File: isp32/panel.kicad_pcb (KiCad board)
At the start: 2 copper layers, 73 x 102 mm, 200 parts, among them J1 BAT1, J10 LoRa_ANT, J12 Micro_SD_Card, J2 Switching, J3 USB_C_Receptacle_USB2.0, J4 ESP_JTAG, J5 GPS_ANT, J6 F0, J7 F1, J9 ANT, M1 Motor_Servo, M2 Motor_Servo, M3 Motor_Servo, M4 Motor_Servo, Q1 BSS138, Q2 BSS138, Q3 IRLML6402, Q4 BSS138, Q5 IRLML6402, Q6 S8050, SW1 RST, SW2 IO0, U1 SC189ZSKTRT, U10 BMP280, U11 MPU-9250, U2 USBLC6-2SC6, U3 STM32G030F6, U4 MP1660GTF-Z, U6 24LC32, U7 NEO-XM, U8 ESP32-S3-WROOM-1U, U9 RFM98W-315S2

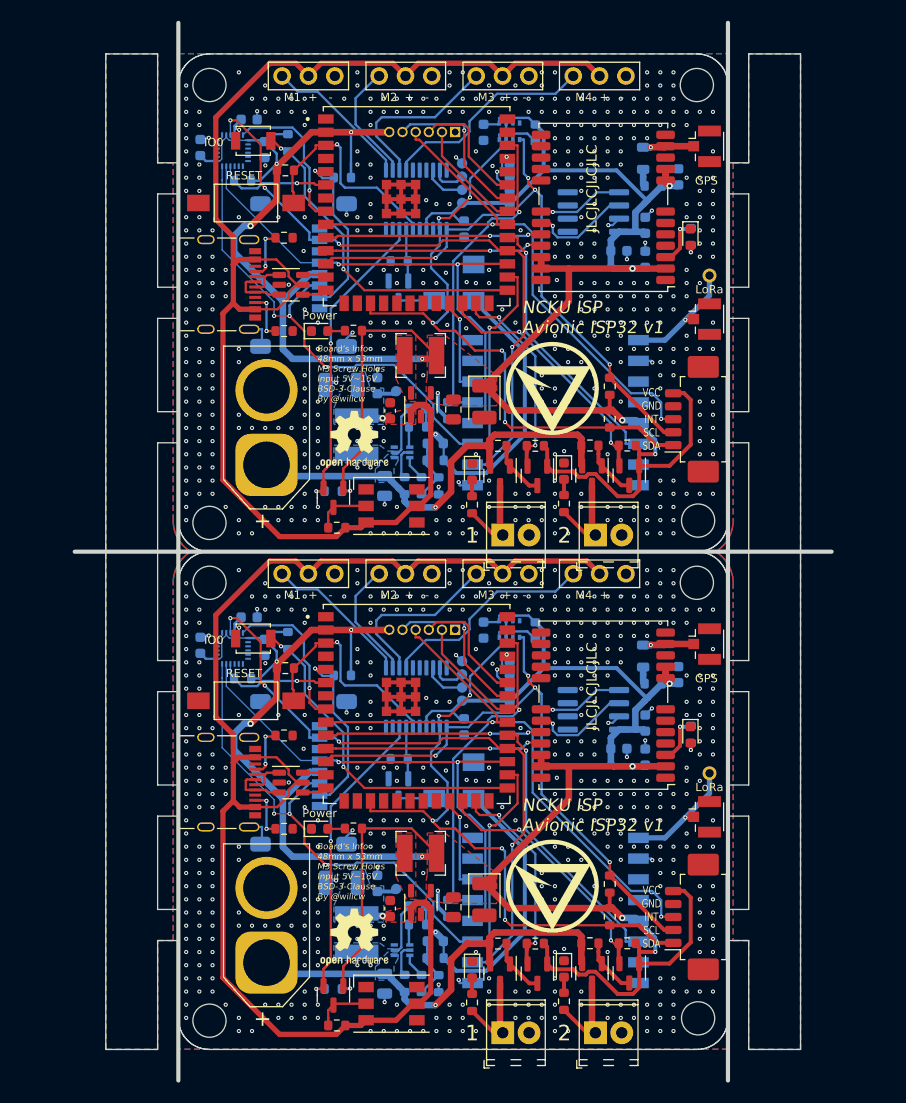
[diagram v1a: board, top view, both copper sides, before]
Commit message: Change label and panel size
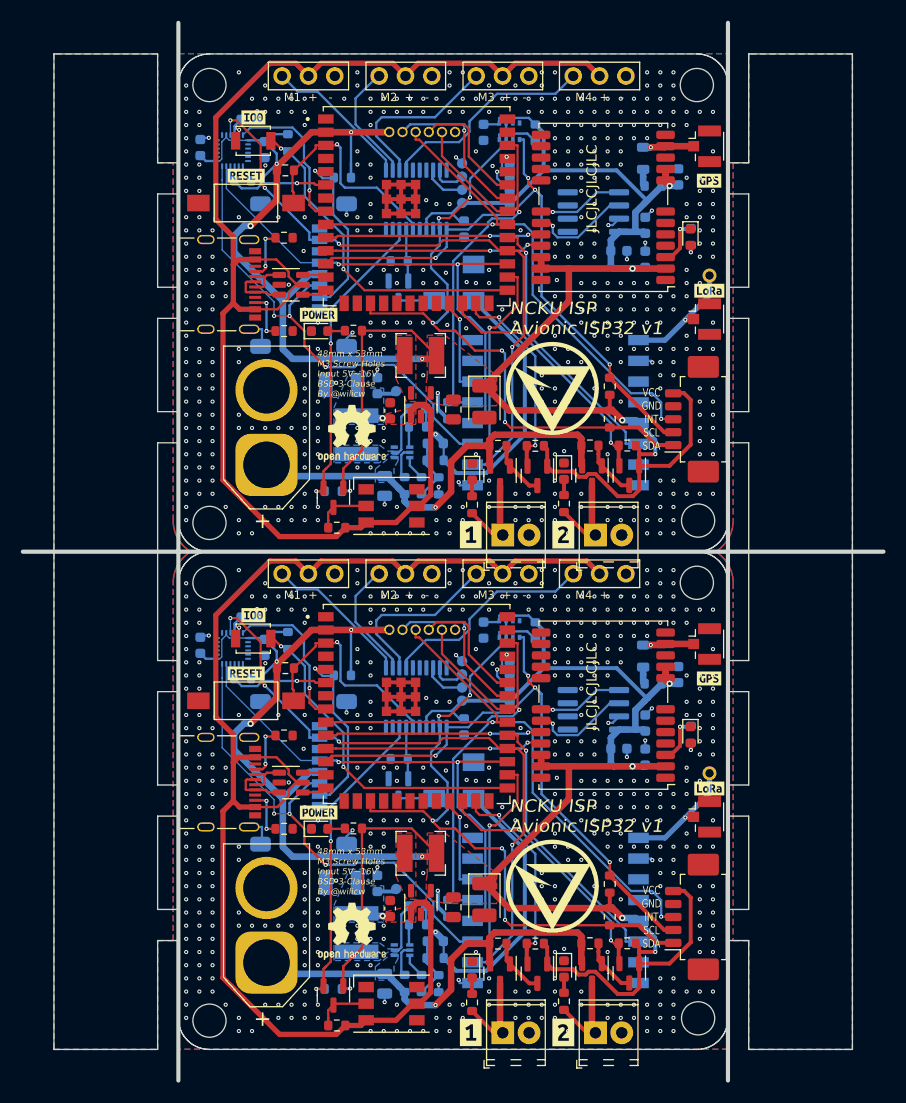
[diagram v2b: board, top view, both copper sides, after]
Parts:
- removed the REF** at (95.5, 57.2)
- removed the REF** at (95.5, 105.2)
- added REF**: OSHW-Logo2_7.3x6mm_SilkScreen, Symbol:OSHW-Logo2_7.3x6mm_SilkScreen, F.Cu at (95.2, 56.6)
- added REF**: OSHW-Logo2_7.3x6mm_SilkScreen, Symbol:OSHW-Logo2_7.3x6mm_SilkScreen, F.Cu at (95.2, 104.6)
- added kibuzzard-63CD04EB: G***, kibuzzard-63CD04EB, F.Cu at (106.7, 114.4)
- added kibuzzard-63CD04EB: G***, kibuzzard-63CD04EB, F.Cu at (106.7, 66.4)
- added kibuzzard-63CD04FB: G***, kibuzzard-63CD04FB, F.Cu at (115.6, 66.4)
- added kibuzzard-63CD04FB: G***, kibuzzard-63CD04FB, F.Cu at (115.6, 114.4)
- added kibuzzard-63CD1CED: G***, kibuzzard-63CD1CED, F.Cu at (85.0, 79.7)
- added kibuzzard-63CD1CED: G***, kibuzzard-63CD1CED, F.Cu at (85.0, 31.7)
- added kibuzzard-63CD1CF7: G***, kibuzzard-63CD1CF7, F.Cu at (85.7, 26.1)
- added kibuzzard-63CD1CF7: G***, kibuzzard-63CD1CF7, F.Cu at (85.7, 74.1)
- added kibuzzard-63CD1D24: G***, kibuzzard-63CD1D24, F.Cu at (92.0, 93.2)
- added kibuzzard-63CD1D24: G***, kibuzzard-63CD1D24, F.Cu at (92.0, 45.2)
- added kibuzzard-63CD1D2E: G***, kibuzzard-63CD1D2E, F.Cu at (129.7, 90.8)
- added kibuzzard-63CD1D2E: G***, kibuzzard-63CD1D2E, F.Cu at (129.7, 42.8)
- added kibuzzard-63CD1D37: G***, kibuzzard-63CD1D37, F.Cu at (129.7, 80.2)
- added kibuzzard-63CD1D37: G***, kibuzzard-63CD1D37, F.Cu at (129.7, 32.2)
- added kibuzzard-63CD1E61: G***, kibuzzard-63CD1E61, B.Cu at (107.8, 82.4)
- added kibuzzard-63CD1E61: G***, kibuzzard-63CD1E61, B.Cu at (112.4, 34.4)
- added kibuzzard-63CD1E61: G***, kibuzzard-63CD1E61, B.Cu at (107.8, 34.4)
- added kibuzzard-63CD1E61: G***, kibuzzard-63CD1E61, B.Cu at (112.4, 82.4)
- added kibuzzard-63CD1E6C: G***, kibuzzard-63CD1E6C, B.Cu at (112.4, 33.1)
- added kibuzzard-63CD1E6C: G***, kibuzzard-63CD1E6C, B.Cu at (112.4, 81.1)
- added kibuzzard-63CD1E76: G***, kibuzzard-63CD1E76, B.Cu at (112.4, 79.9)
- added kibuzzard-63CD1E76: G***, kibuzzard-63CD1E76, B.Cu at (112.4, 31.9)
- added kibuzzard-63CD1E7F: G***, kibuzzard-63CD1E7F, B.Cu at (107.8, 78.5)
- added kibuzzard-63CD1E7F: G***, kibuzzard-63CD1E7F, B.Cu at (107.8, 30.5)
- added kibuzzard-63CD1E7F: G***, kibuzzard-63CD1E7F, B.Cu at (112.4, 30.6)
- added kibuzzard-63CD1E7F: G***, kibuzzard-63CD1E7F, B.Cu at (112.4, 78.6)
- added kibuzzard-63CD1EC0: G***, kibuzzard-63CD1EC0, B.Cu at (107.8, 31.8)
- added kibuzzard-63CD1EC0: G***, kibuzzard-63CD1EC0, B.Cu at (107.8, 79.8)
- added kibuzzard-63CD1EC5: G***, kibuzzard-63CD1EC5, B.Cu at (107.8, 81.1)
- added kibuzzard-63CD1EC5: G***, kibuzzard-63CD1EC5, B.Cu at (107.8, 33.1)
- added kibuzzard-63CD1F56: G***, kibuzzard-63CD1F56, B.Cu at (105.2, 73.6)
- added kibuzzard-63CD1F56: G***, kibuzzard-63CD1F56, B.Cu at (105.2, 25.6)
- added kibuzzard-63CD1F64: G***, kibuzzard-63CD1F64, B.Cu at (103.9, 73.6)
- added kibuzzard-63CD1F64: G***, kibuzzard-63CD1F64, B.Cu at (103.9, 25.6)
- added kibuzzard-63CD1F6A: G***, kibuzzard-63CD1F6A, B.Cu at (102.7, 73.6)
- added kibuzzard-63CD1F6A: G***, kibuzzard-63CD1F6A, B.Cu at (102.7, 25.6)
- added kibuzzard-63CD1F72: G***, kibuzzard-63CD1F72, B.Cu at (101.4, 25.6)
- added kibuzzard-63CD1F72: G***, kibuzzard-63CD1F72, B.Cu at (101.4, 73.6)
- added kibuzzard-63CD1F77: G***, kibuzzard-63CD1F77, B.Cu at (100.1, 25.6)
- added kibuzzard-63CD1F77: G***, kibuzzard-63CD1F77, B.Cu at (100.1, 73.6)
- added kibuzzard-63CD1F7D: G***, kibuzzard-63CD1F7D, B.Cu at (98.8, 25.6)
- added kibuzzard-63CD1F7D: G***, kibuzzard-63CD1F7D, B.Cu at (98.8, 73.6)
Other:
- board size 73 x 102 mm -> 83 x 102 mm
- board text added: "48mm x 53mm M3 Screw Holes Input 5V~16V BSD-3-Clause By @wilicw"
- board text removed: "1"
- board text removed: "2"
- board text removed: "Board's Info 48mm x 53mm M3 Screw Holes Input 5V~16V BSD-3-Clause By @wilicw"
- board text removed: "GND RXD TXD 3V3"
- board text removed: "GND SWCLK SWDIO 3V3"
- board text removed: "GND TDO TMS TCK TDI 3V3"
- board text removed: "GPS"
- board text removed: "IO0"
- board text removed: "LoRa"
- board text removed: "Power"
- board text removed: "RESET"

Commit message: Fix all isp32 issues
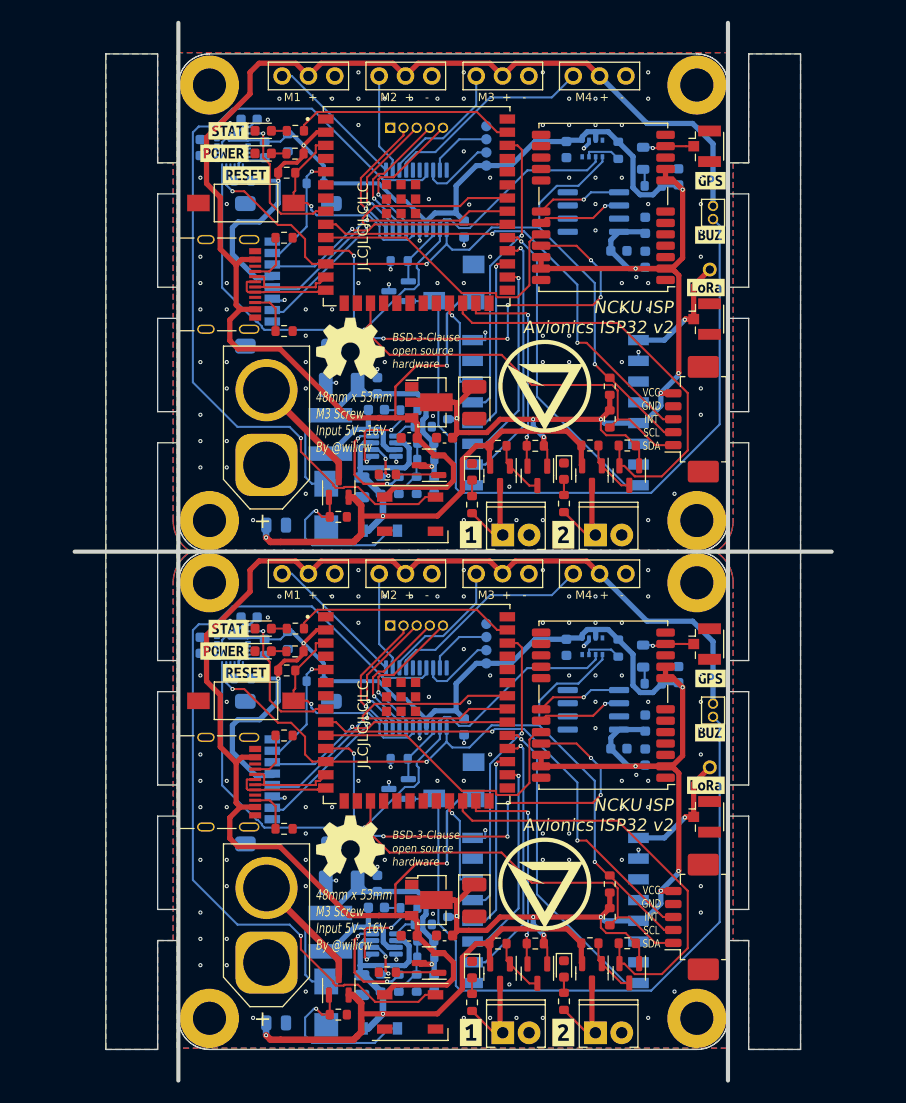
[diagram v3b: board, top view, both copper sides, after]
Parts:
- removed the C1 at (98.9, 102.4)
- removed the C1 at (98.9, 54.4)
- removed the C10 at (108.0, 101.5)
- removed the C10 at (108.0, 53.5)
- removed the C16 at (107.9, 75.6)
- removed the C16 at (107.9, 27.6)
- removed the C4 at (101.6, 102.2)
- removed the C4 at (101.6, 54.2)
- removed the C5 at (98.4, 61.7)
- removed the C5 at (98.4, 109.7)
- removed the C6 at (105.0, 54.3)
- removed the C6 at (105.0, 102.3)
- removed the C7 at (103.3, 105.6)
- removed the C7 at (103.3, 57.6)
- removed the D1 at (127.9, 85.7)
- removed the D1 at (127.9, 37.7)
- removed the D3 at (99.1, 63.6)
- removed the D3 at (99.1, 111.6)
- removed the D5 at (92.1, 46.7)
- removed the D5 at (92.1, 94.7)
- removed the G*** at (114.6, 52.3)
- removed the G*** at (114.6, 100.3)
- removed the H1 at (81.5, 23.0)
- removed the H1 at (81.5, 71.0)
- removed the H2 at (81.5, 113.2)
- removed the H2 at (81.5, 65.2)
- removed the H3 at (128.6, 113.0)
- removed the H3 at (128.6, 65.0)
- removed the H4 at (128.5, 23.0)
- removed the H4 at (128.5, 71.0)
- removed the J12 at (90.0, 41.3)
- removed the J12 at (90.0, 89.3)
- removed the J4 at (105.2, 27.5)
- removed the J4 at (105.2, 75.5)
- removed the J9 at (129.7, 41.4)
- removed the J9 at (129.7, 89.4)
- removed L1 (x2): 1u, Inductor_SMD:L_Bourns-SRN4018
- removed the L3 at (95.7, 56.7)
- removed the L3 at (95.7, 104.7)
- removed the Q2 at (93.5, 62.8)
- removed the Q2 at (93.5, 110.8)
- removed the Q6 at (99.7, 90.8)
- removed the Q6 at (99.7, 42.8)
- removed the R1 at (88.8, 79.2)
- removed the R1 at (88.8, 31.2)
- removed the R10 at (103.6, 61.7)
- removed the R10 at (103.6, 109.7)
- removed the R11 at (103.3, 59.2)
- removed the R11 at (103.3, 107.2)
- removed R13 (x2): 330, Resistor_SMD:R_0603_1608Metric
- removed the R14 at (112.9, 27.6)
- removed the R14 at (112.9, 75.6)
- removed the R18 at (95.4, 94.7)
- removed the R18 at (95.4, 46.7)
- removed the R19 at (93.4, 110.2)
- removed the R19 at (93.4, 62.2)
- removed the R21 at (93.8, 65.7)
- removed the R21 at (93.8, 113.7)
- removed the R3 at (100.3, 109.6)
- removed the R3 at (100.3, 61.6)
- removed the R30 at (94.3, 31.9)
- removed the R30 at (94.3, 79.9)
- removed the R8 at (101.6, 56.0)
- removed the R8 at (101.6, 104.0)
- removed the R9 at (102.0, 109.6)
- removed the R9 at (102.0, 61.6)
- removed the REF** at (95.2, 56.6)
- removed the REF** at (95.2, 104.6)
- removed SW2 (x2): IO0, Button_Switch_SMD:SW_SPST_B3U-1000P
- removed the TP1 at (105.9, 34.4)
- removed the TP1 at (105.9, 82.4)
- removed TP2 (x2): TP5v, TestPoint:TestPoint_Pad_D1.0mm
- removed the TP3 at (105.9, 33.1)
- removed the TP3 at (105.9, 81.1)
- removed the TP4 at (105.9, 31.8)
- removed the TP4 at (105.9, 79.8)
- removed the TP5 at (105.9, 30.6)
- removed the TP5 at (105.9, 78.6)
- removed TP6 (x2): 3V3, TestPoint:TestPoint_Pad_D1.0mm
- removed TP7 (x2): SWDIO, TestPoint:TestPoint_Pad_D1.0mm
- removed TP8 (x2): SWCLK, TestPoint:TestPoint_Pad_D1.0mm
- removed TP9 (x2): GND, TestPoint:TestPoint_Pad_D1.0mm
- removed the U1 at (101.9, 101.8)
- removed the U1 at (101.9, 53.8)
- removed the U10 at (110.4, 75.5)
- removed the U10 at (110.4, 27.5)
- removed the U2 at (89.4, 90.3)
- removed the U2 at (89.4, 42.3)
- removed U4 (x2): MP1660GTF-Z, Package_TO_SOT_SMD:SOT-563
- removed kibuzzard-63CD1CED (x2): G***, kibuzzard-63CD1CED
- removed kibuzzard-63CD1CF7 (x2): G***, kibuzzard-63CD1CF7
- removed kibuzzard-63CD1D24 (x2): G***, kibuzzard-63CD1D24
- removed kibuzzard-63CD1D2E (x2): G***, kibuzzard-63CD1D2E
- removed kibuzzard-63CD1D37 (x2): G***, kibuzzard-63CD1D37
- removed the kibuzzard-63CD1E61 at (107.8, 82.4)
- removed the kibuzzard-63CD1E61 at (112.4, 34.4)
- removed the kibuzzard-63CD1E61 at (107.8, 34.4)
- removed the kibuzzard-63CD1E61 at (112.4, 82.4)
- removed kibuzzard-63CD1E6C (x2): G***, kibuzzard-63CD1E6C
- removed kibuzzard-63CD1E76 (x2): G***, kibuzzard-63CD1E76
- removed the kibuzzard-63CD1E7F at (107.8, 78.5)
- removed the kibuzzard-63CD1E7F at (107.8, 30.5)
- removed the kibuzzard-63CD1E7F at (112.4, 30.6)
- removed the kibuzzard-63CD1E7F at (112.4, 78.6)
- removed the kibuzzard-63CD1EC0 at (107.8, 31.8)
- removed the kibuzzard-63CD1EC0 at (107.8, 79.8)
- removed the kibuzzard-63CD1EC5 at (107.8, 81.1)
- removed the kibuzzard-63CD1EC5 at (107.8, 33.1)
- removed kibuzzard-63CD1F56 (x2): G***, kibuzzard-63CD1F56
- removed kibuzzard-63CD1F64 (x2): G***, kibuzzard-63CD1F64
- removed kibuzzard-63CD1F6A (x2): G***, kibuzzard-63CD1F6A
- removed kibuzzard-63CD1F72 (x2): G***, kibuzzard-63CD1F72
- removed kibuzzard-63CD1F77 (x2): G***, kibuzzard-63CD1F77
- removed kibuzzard-63CD1F7D (x2): G***, kibuzzard-63CD1F7D
- added C1: 22u, Capacitor_SMD:C_0603_1608Metric, B.Cu at (103.2, 61.6)
- added C1: 22u, Capacitor_SMD:C_0603_1608Metric, B.Cu at (103.2, 109.6)
- added C10: 22u, Capacitor_SMD:C_0603_1608Metric, F.Cu at (104.2, 57.0)
- added C10: 22u, Capacitor_SMD:C_0603_1608Metric, F.Cu at (104.2, 105.0)
- added C12: 220u, Capacitor_Tantalum_SMD:CP_EIA-3528-12_Kemet-T, F.Cu at (107.0, 53.6)
- added C12: 220u, Capacitor_Tantalum_SMD:CP_EIA-3528-12_Kemet-T, F.Cu at (107.0, 101.6)
- added C15: 10u, Capacitor_SMD:C_0805_2012Metric, B.Cu at (87.9, 113.4)
- added C15: 10u, Capacitor_SMD:C_0805_2012Metric, B.Cu at (87.9, 65.4)
- added C16: 100n, Capacitor_SMD:C_0603_1608Metric, B.Cu at (115.9, 77.2)
- added C16: 100n, Capacitor_SMD:C_0603_1608Metric, B.Cu at (115.9, 29.2)
- added C4: 100n, Capacitor_SMD:C_0603_1608Metric, B.Cu at (97.6, 54.3)
- added C4: 100n, Capacitor_SMD:C_0603_1608Metric, B.Cu at (97.6, 102.3)
- added C5: 100n, Capacitor_SMD:C_0805_2012Metric, B.Cu at (96.2, 61.8)
- added C5: 100n, Capacitor_SMD:C_0805_2012Metric, B.Cu at (96.2, 109.8)
- added C6: 22u, Capacitor_SMD:C_0603_1608Metric, F.Cu at (100.8, 57.0)
- added C6: 22u, Capacitor_SMD:C_0603_1608Metric, F.Cu at (100.8, 105.0)
- added C7: NC, Capacitor_SMD:C_0603_1608Metric, B.Cu at (102.4, 57.5)
- added C7: NC, Capacitor_SMD:C_0603_1608Metric, B.Cu at (102.4, 105.5)
- added D1: Zener, Diode_SMD:D_SOD-123, B.Cu at (98.0, 114.0)
- added D1: Zener, Diode_SMD:D_SOD-123, B.Cu at (98.0, 66.0)
- added D3: ESP_LED, LED_SMD:LED_0603_1608Metric, F.Cu at (86.7, 75.4)
- added D3: ESP_LED, LED_SMD:LED_0603_1608Metric, F.Cu at (86.7, 27.4)
- added D5: POWER, LED_SMD:LED_0603_1608Metric, F.Cu at (86.7, 77.6)
- added D5: POWER, LED_SMD:LED_0603_1608Metric, F.Cu at (86.7, 29.6)
- added D6: TVS, Diode_SMD:D_SMB, B.Cu at (92.8, 111.6)
- added D6: TVS, Diode_SMD:D_SMB, B.Cu at (92.8, 63.6)
- added D7: WS2812B, LED_SMD:LED_WS2812B_PLCC4_5.0x5.0mm_P3.2mm, F.Cu at (100.8, 64.4)
- added D7: WS2812B, LED_SMD:LED_WS2812B_PLCC4_5.0x5.0mm_P3.2mm, F.Cu at (100.8, 112.4)
- added G***: LOGO, isp_logo:isp_logo, F.Cu at (113.8, 100.0)
- added G***: LOGO, isp_logo:isp_logo, F.Cu at (113.8, 52.0)
- added H1: MountingHole_Pad, MountingHole:MountingHole_3.2mm_M3_ISO7380_Pad, F.Cu at (81.5, 23.0)
- added H1: MountingHole_Pad, MountingHole:MountingHole_3.2mm_M3_ISO7380_Pad, F.Cu at (81.5, 71.0)
- added H2: MountingHole_Pad, MountingHole:MountingHole_3.2mm_M3_ISO7380_Pad, F.Cu at (81.5, 113.0)
- added H2: MountingHole_Pad, MountingHole:MountingHole_3.2mm_M3_ISO7380_Pad, F.Cu at (81.5, 65.0)
- added H3: MountingHole_Pad, MountingHole:MountingHole_3.2mm_M3_ISO7380_Pad, F.Cu at (128.5, 65.0)
- added H3: MountingHole_Pad, MountingHole:MountingHole_3.2mm_M3_ISO7380_Pad, F.Cu at (128.5, 113.0)
- added H4: MountingHole_Pad, MountingHole:MountingHole_3.2mm_M3_ISO7380_Pad, F.Cu at (128.5, 23.0)
- added H4: MountingHole_Pad, MountingHole:MountingHole_3.2mm_M3_ISO7380_Pad, F.Cu at (128.5, 71.0)
- added J12: Micro_SD_Card, Connector_Card:microSD_HC_Molex_47219-2001, B.Cu at (89.7, 41.3)
- added J12: Micro_SD_Card, Connector_Card:microSD_HC_Molex_47219-2001, B.Cu at (89.7, 89.3)
- added J4: ADC, Connector_PinHeader_1.27mm:PinHeader_1x05_P1.27mm_Vertical, B.Cu at (104.0, 75.1)
- added J4: ADC, Connector_PinHeader_1.27mm:PinHeader_1x05_P1.27mm_Vertical, B.Cu at (104.0, 27.1)
- added J8: BUZZ, Connector_PinHeader_1.27mm:PinHeader_1x02_P1.27mm_Vertical, F.Cu at (130.1, 34.7)
- added J8: BUZZ, Connector_PinHeader_1.27mm:PinHeader_1x02_P1.27mm_Vertical, F.Cu at (130.1, 82.7)
- added J9: ANT, Connector_PinHeader_2.00mm:PinHeader_1x01_P2.00mm_Vertical, F.Cu at (129.7, 88.8)
- added J9: ANT, Connector_PinHeader_2.00mm:PinHeader_1x01_P2.00mm_Vertical, F.Cu at (129.7, 40.8)
- added L3: 5.5, Inductor_SMD:L_Sunlord_SWPA5020S, B.Cu at (93.2, 56.7)
- added L3: 5.5, Inductor_SMD:L_Sunlord_SWPA5020S, B.Cu at (93.2, 104.7)
- added Q2: S8050, Package_TO_SOT_SMD:SOT-23, B.Cu at (99.7, 42.9)
- added Q2: S8050, Package_TO_SOT_SMD:SOT-23, B.Cu at (99.7, 90.9)
- added Q6: IRLML6402, Package_TO_SOT_SMD:SOT-23, F.Cu at (94.0, 61.8)
- added Q6: IRLML6402, Package_TO_SOT_SMD:SOT-23, F.Cu at (94.0, 109.8)
- added Q7: IRLML6402, Package_TO_SOT_SMD:SOT-23, F.Cu at (102.7, 107.7)
- added Q7: IRLML6402, Package_TO_SOT_SMD:SOT-23, F.Cu at (102.7, 59.7)
- added R1: 10k, Resistor_SMD:R_0603_1608Metric, F.Cu at (88.9, 79.5)
- added R1: 10k, Resistor_SMD:R_0603_1608Metric, F.Cu at (88.9, 31.5)
- added R10: 7k5, Resistor_SMD:R_0603_1608Metric, B.Cu at (101.5, 109.6)
- added R10: 7k5, Resistor_SMD:R_0603_1608Metric, B.Cu at (101.5, 61.6)
- added R11: 40.2k, Resistor_SMD:R_0603_1608Metric, B.Cu at (102.4, 59.1)
- added R11: 40.2k, Resistor_SMD:R_0603_1608Metric, B.Cu at (102.4, 107.1)
- added R14: 10k, Resistor_SMD:R_0603_1608Metric, B.Cu at (120.9, 29.3)
- added R14: 10k, Resistor_SMD:R_0603_1608Metric, B.Cu at (120.9, 77.3)
- added R18: 1k, Resistor_SMD:R_0603_1608Metric, F.Cu at (89.7, 77.6)
- added R18: 1k, Resistor_SMD:R_0603_1608Metric, F.Cu at (89.7, 29.6)
- added R19: 1k, Resistor_SMD:R_0603_1608Metric, F.Cu at (89.8, 27.4)
- added R19: 1k, Resistor_SMD:R_0603_1608Metric, F.Cu at (89.8, 75.4)
- added R21: 75k, Resistor_SMD:R_0603_1608Metric, B.Cu at (102.1, 103.9)
- added R21: 75k, Resistor_SMD:R_0603_1608Metric, B.Cu at (102.1, 55.9)
- added R26: 100k, Resistor_SMD:R_0603_1608Metric, F.Cu at (93.9, 112.6)
- added R26: 100k, Resistor_SMD:R_0603_1608Metric, F.Cu at (93.9, 64.6)
- added R27: 100k, Resistor_SMD:R_0603_1608Metric, F.Cu at (98.7, 60.6)
- added R27: 100k, Resistor_SMD:R_0603_1608Metric, F.Cu at (98.7, 108.6)
- added R3: 100k, Resistor_SMD:R_0603_1608Metric, B.Cu at (98.0, 61.6)
- added R3: 100k, Resistor_SMD:R_0603_1608Metric, B.Cu at (98.0, 109.6)
- added R30: 10k, Resistor_SMD:R_0603_1608Metric, B.Cu at (91.7, 80.5)
- added R30: 10k, Resistor_SMD:R_0603_1608Metric, B.Cu at (91.7, 32.5)
- added R8: 20, Resistor_SMD:R_0603_1608Metric, B.Cu at (100.7, 102.4)
- added R8: 20, Resistor_SMD:R_0603_1608Metric, B.Cu at (100.7, 54.4)
- added R9: 20k, Resistor_SMD:R_0603_1608Metric, B.Cu at (99.8, 109.6)
- added R9: 20k, Resistor_SMD:R_0603_1608Metric, B.Cu at (99.8, 61.6)
- added REF**: OSHW-Symbol_6.7x6mm_SilkScreen, Symbol:OSHW-Symbol_6.7x6mm_SilkScreen, F.Cu at (95.1, 96.4)
- added REF**: OSHW-Symbol_6.7x6mm_SilkScreen, Symbol:OSHW-Symbol_6.7x6mm_SilkScreen, F.Cu at (95.1, 48.4)
- added TP1: 3V3, TestPoint:TestPoint_Pad_D1.0mm, B.Cu at (108.2, 30.8)
- added TP1: 3V3, TestPoint:TestPoint_Pad_D1.0mm, B.Cu at (108.2, 78.8)
- added TP3: SWDIO, TestPoint:TestPoint_Pad_D1.0mm, B.Cu at (108.2, 77.5)
- added TP3: SWDIO, TestPoint:TestPoint_Pad_D1.0mm, B.Cu at (108.2, 29.5)
- added TP4: SWCLK, TestPoint:TestPoint_Pad_D1.0mm, B.Cu at (108.2, 28.2)
- added TP4: SWCLK, TestPoint:TestPoint_Pad_D1.0mm, B.Cu at (108.2, 76.2)
- added TP5: GND, TestPoint:TestPoint_Pad_D1.0mm, B.Cu at (108.2, 75.0)
- added TP5: GND, TestPoint:TestPoint_Pad_D1.0mm, B.Cu at (108.2, 27.0)
- added U1: AZ1117-3.3, Package_TO_SOT_SMD:SOT-89-3, F.Cu at (102.6, 101.6)
- added U1: AZ1117-3.3, Package_TO_SOT_SMD:SOT-89-3, F.Cu at (102.6, 53.6)
- added U10: BMP280, Package_LGA:Bosch_LGA-8_2x2.5mm_P0.65mm_ClockwisePinNumbering, B.Cu at (118.4, 77.1)
- added U10: BMP280, Package_LGA:Bosch_LGA-8_2x2.5mm_P0.65mm_ClockwisePinNumbering, B.Cu at (118.4, 29.1)
- added U2: MP2315, Package_TO_SOT_SMD:TSOT-23-8, B.Cu at (98.3, 57.8)
- added U2: MP2315, Package_TO_SOT_SMD:TSOT-23-8, B.Cu at (98.3, 105.8)
- added kibuzzard-63CD1E61: G***, kibuzzard-63CD1E61, B.Cu at (110.1, 30.8)
- added kibuzzard-63CD1E61: G***, kibuzzard-63CD1E61, B.Cu at (110.1, 78.8)
- added kibuzzard-63CD1E7F: G***, kibuzzard-63CD1E7F, B.Cu at (110.1, 74.9)
- added kibuzzard-63CD1E7F: G***, kibuzzard-63CD1E7F, B.Cu at (110.1, 26.9)
- added kibuzzard-63CD1EC0: G***, kibuzzard-63CD1EC0, B.Cu at (110.1, 76.2)
- added kibuzzard-63CD1EC0: G***, kibuzzard-63CD1EC0, B.Cu at (110.1, 28.2)
- added kibuzzard-63CD1EC5: G***, kibuzzard-63CD1EC5, B.Cu at (110.1, 77.5)
- added kibuzzard-63CD1EC5: G***, kibuzzard-63CD1EC5, B.Cu at (110.1, 29.5)
- added kibuzzard-641A737F: G***, kibuzzard-641A737F, F.Cu at (85.0, 79.7)
- added kibuzzard-641A737F: G***, kibuzzard-641A737F, F.Cu at (85.0, 31.7)
- added kibuzzard-641A7395: G***, kibuzzard-641A7395, F.Cu at (129.8, 32.2)
- added kibuzzard-641A7395: G***, kibuzzard-641A7395, F.Cu at (129.8, 80.2)
- added kibuzzard-641A73AC: G***, kibuzzard-641A73AC, F.Cu at (129.4, 42.5)
- added kibuzzard-641A73AC: G***, kibuzzard-641A73AC, F.Cu at (129.4, 90.5)
- added kibuzzard-641A73E5: G***, kibuzzard-641A73E5, F.Cu at (83.3, 75.4)
- added kibuzzard-641A73E5: G***, kibuzzard-641A73E5, F.Cu at (83.3, 27.4)
- added kibuzzard-641A73FA: G***, kibuzzard-641A73FA, F.Cu at (82.9, 29.6)
- added kibuzzard-641A73FA: G***, kibuzzard-641A73FA, F.Cu at (82.9, 77.6)
- added kibuzzard-641A7704: G***, kibuzzard-641A7704, F.Cu at (129.8, 37.5)
- added kibuzzard-641A7704: G***, kibuzzard-641A7704, F.Cu at (129.8, 85.5)
- L2 (x2): value 22u -> NC
- R12 (x2): value 22 -> NC
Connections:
- C2 pad 1: Board_1-+5V -> Board_1-Net-(C1-Pad1)
- C2 pad 1: Board_0-+5V -> Board_0-Net-(C1-Pad1)
- C8 pad 1: Board_0-+5V -> Board_0-Net-(C1-Pad1)
- C8 pad 1: Board_1-+5V -> Board_1-Net-(C1-Pad1)
- J1 pad 1: Board_0-+BATT -> Board_0-GND
- J1 pad 2: Board_0-GND -> Board_0-Net-(D6-Pad2)
- J1 pad 1: Board_1-+BATT -> Board_1-GND
- J1 pad 2: Board_1-GND -> Board_1-Net-(D6-Pad2)
- J3 pad A6: Board_0-UD+ -> Board_0-D+
- J3 pad A7: Board_0-UD- -> Board_0-D-
- J3 pad B6: Board_0-UD+ -> Board_0-D+
- J3 pad B7: Board_0-UD- -> Board_0-D-
- J3 pad A6: Board_1-UD+ -> Board_1-D+
- J3 pad A7: Board_1-UD- -> Board_1-D-
- J3 pad B6: Board_1-UD+ -> Board_1-D+
- J3 pad B7: Board_1-UD- -> Board_1-D-
- LS1 pad N: Board_0-Net-(LS1-PadN) -> Board_0-Net-(J8-Pad2)
- LS1 pad N: Board_1-Net-(LS1-PadN) -> Board_1-Net-(J8-Pad2)
- U11 pad 22: Board_0-IMU_SS -> Board_0-unconnected-(U11-Pad22)
- U11 pad 23: Board_0-SCK -> Board_0-SCL
- U11 pad 24: Board_0-MOSI -> Board_0-SDA
- U11 pad 9: Board_0-MISO -> Board_0-unconnected-(U11-Pad9)
- U11 pad 22: Board_1-IMU_SS -> Board_1-unconnected-(U11-Pad22)
- U11 pad 23: Board_1-SCK -> Board_1-SCL
- U11 pad 24: Board_1-MOSI -> Board_1-SDA
- U11 pad 9: Board_1-MISO -> Board_1-unconnected-(U11-Pad9)
- U3 pad 10: Board_1-unconnected-(U3-Pad10) -> Board_1-ADC3
- U3 pad 17: Board_1-unconnected-(U3-Pad17) -> Board_1-RGB
- U3 pad 3: Board_1-unconnected-(U3-Pad3) -> Board_1-Buzz
- U3 pad 7: Board_1-Buzz -> Board_1-ADC0
- U3 pad 8: Board_1-RGB -> Board_1-ADC1
- U3 pad 9: Board_1-unconnected-(U3-Pad9) -> Board_1-ADC2
- U3 pad 10: Board_0-unconnected-(U3-Pad10) -> Board_0-ADC3
- U3 pad 17: Board_0-unconnected-(U3-Pad17) -> Board_0-RGB
- U3 pad 3: Board_0-unconnected-(U3-Pad3) -> Board_0-Buzz
- U3 pad 7: Board_0-Buzz -> Board_0-ADC0
- U3 pad 8: Board_0-RGB -> Board_0-ADC1
- U3 pad 9: Board_0-unconnected-(U3-Pad9) -> Board_0-ADC2
- U7 pad 3: Board_1-Net-(R13-Pad1) -> Board_1-unconnected-(U7-Pad3)
- U7 pad 3: Board_0-Net-(R13-Pad1) -> Board_0-unconnected-(U7-Pad3)
- U8 pad 27: Board_0-IO0 -> Board_0-unconnected-(U8-Pad27)
- U8 pad 28: Board_0-MOSI -> Board_0-MOSI_1
- U8 pad 29: Board_0-SCK -> Board_0-SCK_1
- U8 pad 30: Board_0-MISO -> Board_0-MISO_1
- U8 pad 31: Board_0-LORA_INT -> Board_0-LORA_BUSY
- U8 pad 32: Board_0-TCK -> Board_0-MOSI_2
- U8 pad 33: Board_0-TDO -> Board_0-SCK_2
- U8 pad 34: Board_0-TDI -> Board_0-MISO_2
- U8 pad 35: Board_0-TMS -> Board_0-unconnected-(U8-Pad35)
- U8 pad 36: Board_0-TX -> Board_0-unconnected-(U8-Pad36)
- U8 pad 37: Board_0-RX -> Board_0-unconnected-(U8-Pad37)
- U8 pad 39: Board_0-unconnected-(U8-Pad39) -> Board_0-INDI
- U8 pad 6: Board_0-IMU_SS -> Board_0-unconnected-(U8-Pad6)
- U8 pad 27: Board_1-IO0 -> Board_1-unconnected-(U8-Pad27)
- U8 pad 28: Board_1-MOSI -> Board_1-MOSI_1
- U8 pad 29: Board_1-SCK -> Board_1-SCK_1
- U8 pad 30: Board_1-MISO -> Board_1-MISO_1
- U8 pad 31: Board_1-LORA_INT -> Board_1-LORA_BUSY
- U8 pad 32: Board_1-TCK -> Board_1-MOSI_2
- U8 pad 33: Board_1-TDO -> Board_1-SCK_2
- U8 pad 34: Board_1-TDI -> Board_1-MISO_2
- U8 pad 35: Board_1-TMS -> Board_1-unconnected-(U8-Pad35)
- U8 pad 36: Board_1-TX -> Board_1-unconnected-(U8-Pad36)
- U8 pad 37: Board_1-RX -> Board_1-unconnected-(U8-Pad37)
- U8 pad 39: Board_1-unconnected-(U8-Pad39) -> Board_1-INDI
- U8 pad 6: Board_1-IMU_SS -> Board_1-unconnected-(U8-Pad6)
- U9 pad 14: Board_0-LORA_INT -> Board_0-unconnected-(U9-Pad14)
- U9 pad 16: Board_0-unconnected-(U9-Pad16) -> Board_0-LORA_BUSY
- U9 pad 2: Board_0-MISO -> Board_0-MISO_1
- U9 pad 3: Board_0-MOSI -> Board_0-MOSI_1
- U9 pad 4: Board_0-SCK -> Board_0-SCK_1
- U9 pad 14: Board_1-LORA_INT -> Board_1-unconnected-(U9-Pad14)
- U9 pad 16: Board_1-unconnected-(U9-Pad16) -> Board_1-LORA_BUSY
- U9 pad 2: Board_1-MISO -> Board_1-MISO_1
- U9 pad 3: Board_1-MOSI -> Board_1-MOSI_1
- U9 pad 4: Board_1-SCK -> Board_1-SCK_1
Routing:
- net Board_1-Net-(J8-Pad2): track 0.00 -> 69.9 mm
- net Board_0-Net-(J8-Pad2): track 0.00 -> 69.9 mm
- net Board_1-MOSI: track 67.2 -> 0.00 mm, vias 4 -> 0
- net Board_0-MOSI: track 67.2 -> 0.00 mm, vias 4 -> 0
- net Board_0-MISO: track 61.0 -> 0.00 mm, vias 4 -> 0
- net Board_1-MISO: track 61.0 -> 0.00 mm, vias 4 -> 0
- net Board_1-+3V3: track 246.6 -> 192.0 mm
- net Board_0-+3V3: track 246.6 -> 192.0 mm
- net Board_0-SCK: track 50.2 -> 0.00 mm, vias 2 -> 0
- net Board_1-SCK: track 50.2 -> 0.00 mm, vias 2 -> 0
- net Board_0-RGB: track 30.6 -> 80.6 mm, vias 2 -> 1
- net Board_1-RGB: track 30.6 -> 80.6 mm, vias 2 -> 1
- net Board_0-SDA: track 63.0 -> 99.7 mm, vias 5 -> 1
- net Board_1-SDA: track 63.0 -> 99.7 mm, vias 5 -> 1
- net Board_0-IO0: track 32.3 -> 0.00 mm, vias 2 -> 0
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- removed copper zone on F.Cu, net Board_0-+3V3
- removed copper zone on B.Cu, net Board_0-+5V
- removed copper zone on F.Cu, net Board_0-+5V
- removed copper zone on B.Cu, net Board_0-+BATT
- removed copper zone on B.Cu, net Board_0-Net-(C4-Pad2)
- removed copper zone on F.Cu, net Board_0-Net-(L1-Pad1)
- removed copper zone on F.Cu, net Board_1-+3V3
- removed copper zone on B.Cu, net Board_1-+5V
- removed copper zone on F.Cu, net Board_1-+5V
- removed copper zone on B.Cu, net Board_1-+BATT
- removed copper zone on B.Cu, net Board_1-Net-(C4-Pad2)
- removed copper zone on F.Cu, net Board_1-Net-(L1-Pad1)
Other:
- board size 83 x 102 mm -> 73 x 102 mm
- board text added: "48mm x 53mm M3 Screw Input 5V~16V By @wilicw"
- board text added: "A0 A1 A2 A3 AG"
- board text added: "BSD-3-Clause open source hardware"
- board text added: "NCKU ISP Avionics ISP32 v2"
- board text removed: "48mm x 53mm M3 Screw Holes Input 5V~16V BSD-3-Clause By @wilicw"
- board text removed: "5v"
- board text removed: "NCKU ISP Avionic ISP32 v1"
